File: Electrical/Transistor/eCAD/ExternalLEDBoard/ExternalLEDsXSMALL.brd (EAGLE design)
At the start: 49.5 x 33 mm, 7 parts

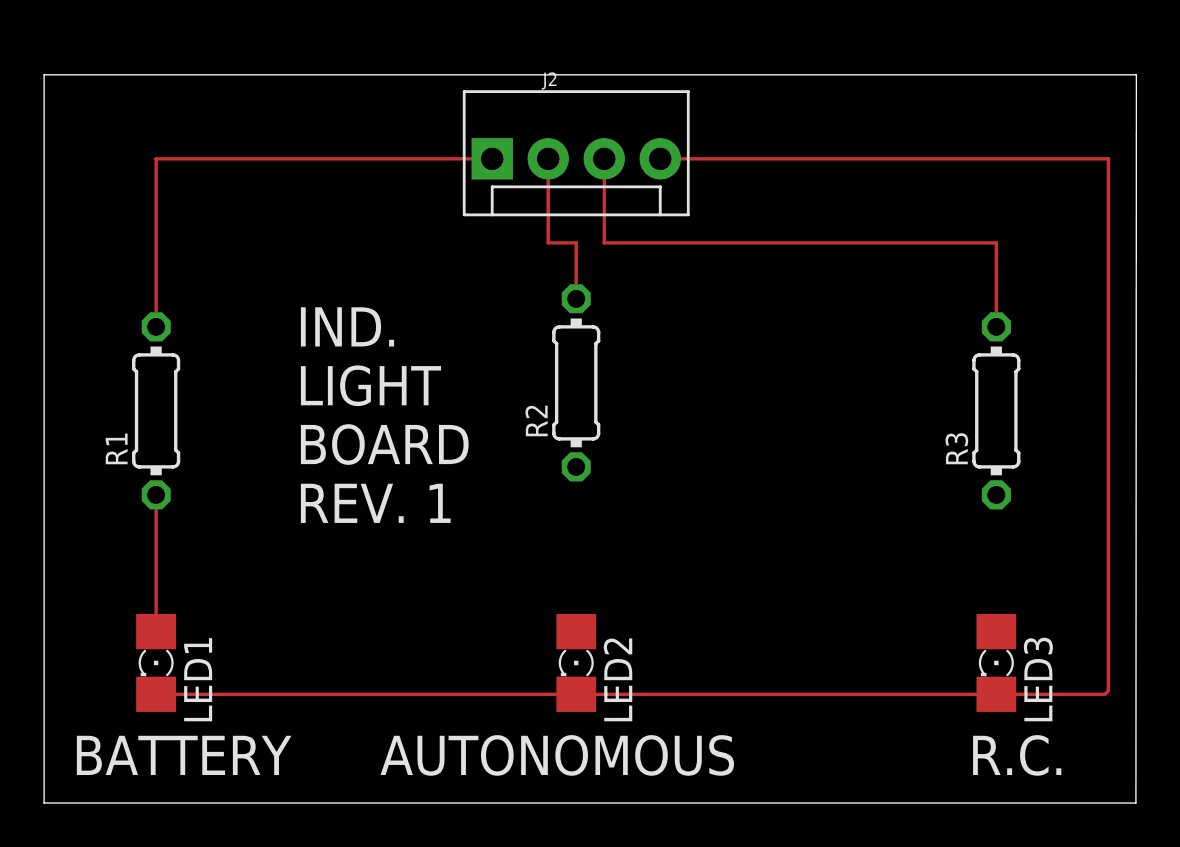
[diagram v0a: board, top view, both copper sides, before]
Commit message: Added smaller boards
There are now two versions of the external LED board. Both have components pushed closer together than on previous versions. The regular version retains spacing and full labels. The XSMALL version is as compact as possible.
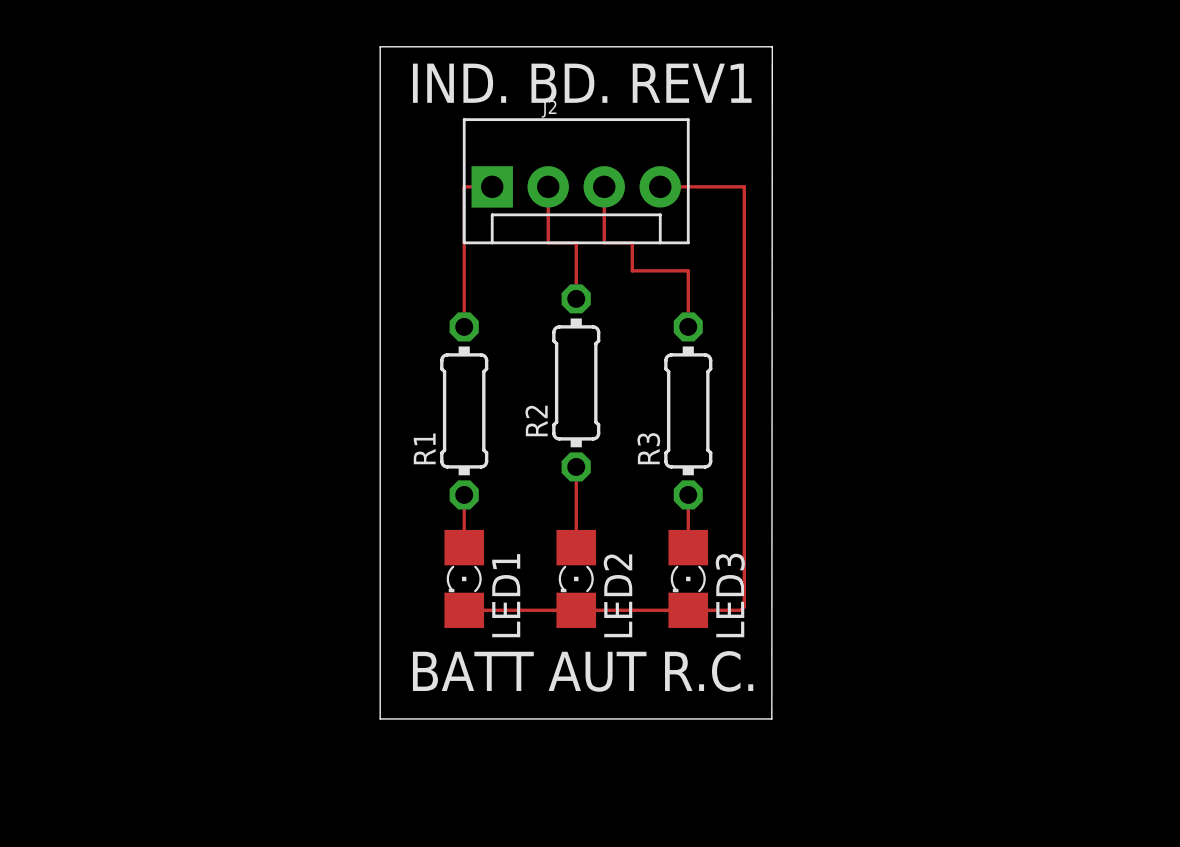
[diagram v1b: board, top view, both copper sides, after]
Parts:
- moved LED1 14.5 mm to (99.1, 35.6)
- moved LED3 14.5 mm to (109.2, 35.6)
- moved R1 14.0 mm to (99.1, 43.2)
- moved R3 14.0 mm to (109.2, 43.2)
- moved LED2 3.81 mm to (104.1, 35.6)
- moved J2 1.27 mm to (100.3, 53.3)
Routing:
- net N$7: track 87.9 -> 35.8 mm
- net N$3: track 25.4 -> 10.2 mm
- net N$1: track 22.9 -> 7.62 mm
- net N$5: track 0.00 -> 3.81 mm
- net N$4: track 6.20 -> 2.39 mm
- net N$6: track 0.00 -> 2.39 mm
- net N$2: track 7.62 -> 6.35 mm
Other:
- board size 49.5 x 33 mm -> 17.8 x 30.5 mm
- board text added: "AUT"
- board text added: "BATT"
- board text added: "IND. BD. REV1"
- board text removed: "AUTONOMOUS"
- board text removed: "BATTERY"
- board text removed: "IND. LIGHT BOARD REV. 1"

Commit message: Increased margins/tolerances on XSMALL version.
Now the LED labels are a little further from the actual LEDs, and there is some margin on each side of the Revision Label.
Revision Label is also on the back now, allowing us to reduce cost by 7.5 cents.
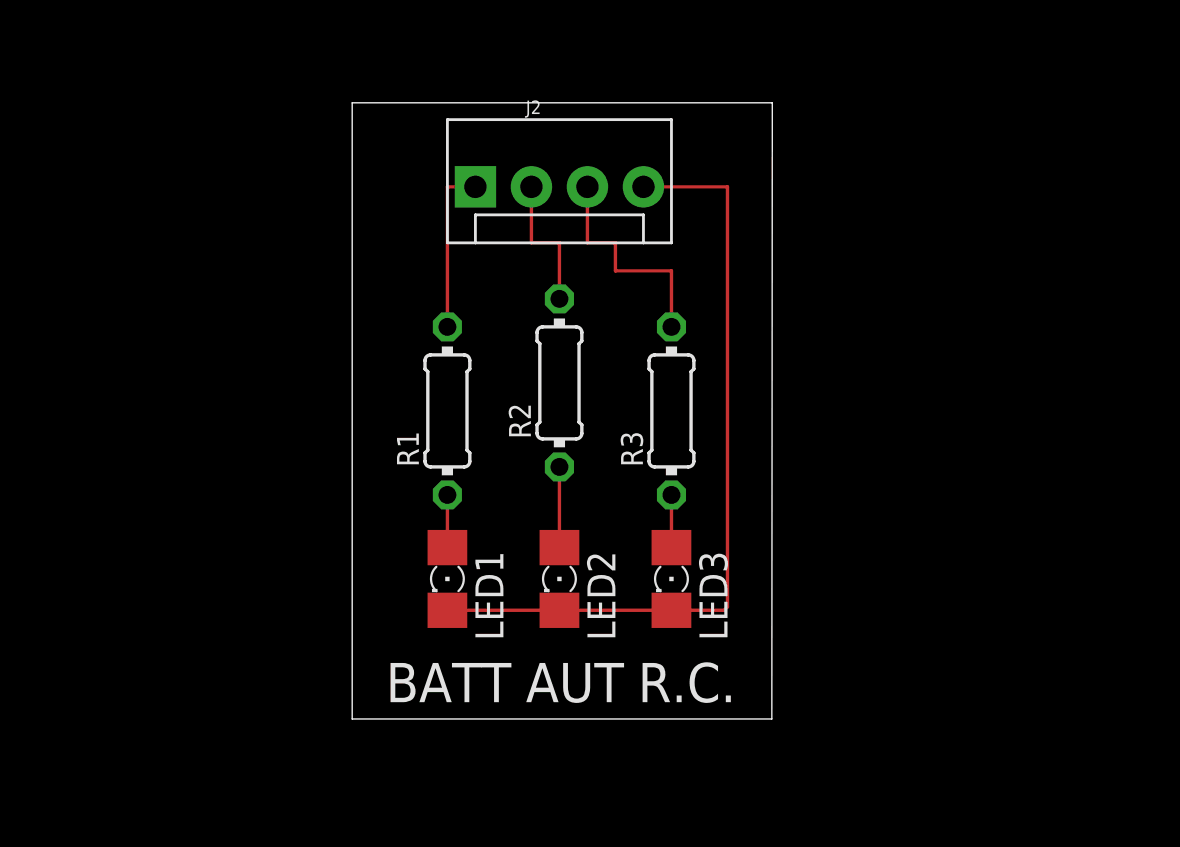
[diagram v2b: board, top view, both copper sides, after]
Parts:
- moved J2 0.76 mm to (99.6, 53.3)
- moved LED1 0.76 mm to (98.3, 35.6)
- moved LED2 0.76 mm to (103.4, 35.6)
- moved LED3 0.76 mm to (108.5, 35.6)
- moved R1 0.76 mm to (98.3, 43.2)
- moved R2 0.76 mm to (103.4, 44.5)
- moved R3 0.76 mm to (108.5, 43.2)
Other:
- board size 17.8 x 30.5 mm -> 19 x 27.9 mm
